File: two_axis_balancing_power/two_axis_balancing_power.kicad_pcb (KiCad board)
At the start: 4 copper layers, 50 x 42.9 mm, 26 parts, among them J1 Conn_01x02, J2 Conn_02x05, J3 Conn_01x02, Q1 AO3401A, U1 RPL-1.0-R, U2 LM393, U3 TB6612FNG

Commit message: Almost finished pcb
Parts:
- added REF**: MountingHole_2.2mm_M2, MountingHole:MountingHole_2.2mm_M2, F.Cu at (174.2, 87.2)
- added REF**: MountingHole_2.2mm_M2, MountingHole:MountingHole_2.2mm_M2, F.Cu at (131.2, 87.2)
- added REF**: MountingHole_2.2mm_M2, MountingHole:MountingHole_2.2mm_M2, F.Cu at (174.2, 122.8)
- added REF**: MountingHole_2.2mm_M2, MountingHole:MountingHole_2.2mm_M2, F.Cu at (131.2, 122.8)
- moved J3 7.82 mm to (138.5, 93.7), turned to -90 degrees
- moved C6 3.54 mm to (152.4, 88.1), turned to -90 degrees
- moved C5 3.51 mm to (154.3, 88.0), turned to -90 degrees
- moved C2 2.63 mm to (151.3, 94.8)
- moved U3 2.63 mm to (146.7, 89.8)
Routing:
- net +5V: track 93.2 -> 87.6 mm
- net /MOTOR_N: track 7.73 -> 11.3 mm
- net /AIN2: track 34.3 -> 30.8 mm
- net /STBY: track 33.5 -> 31.2 mm
- net /PWMA: track 29.8 -> 27.8 mm
- net /MOTOR_P: track 9.99 -> 11.0 mm
- net /AIN1: track 27.8 -> 28.6 mm
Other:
- outline, holes or cut-outs redrawn

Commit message: Finished pcb
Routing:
- net GND: track 2.98 -> 120.5 mm, vias 2 -> 81

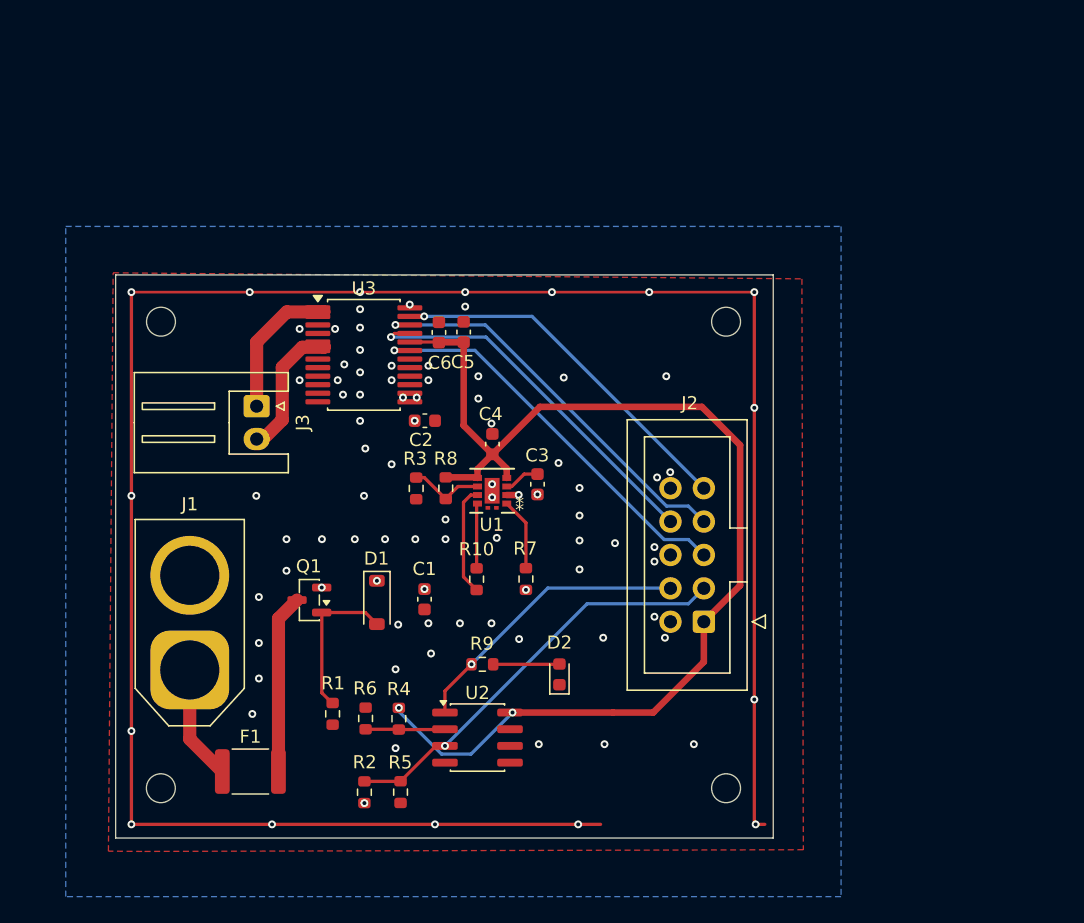
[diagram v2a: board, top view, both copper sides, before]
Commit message: Carrier schematic finished and power board polished
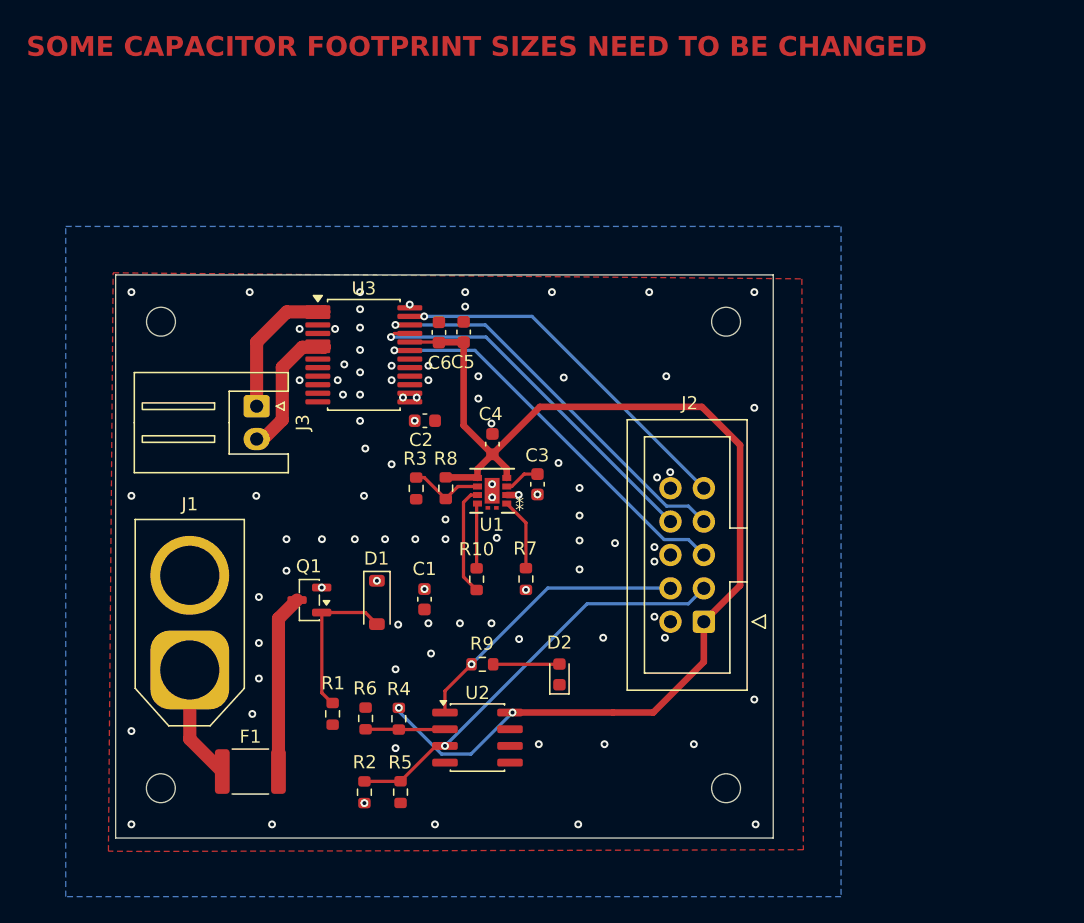
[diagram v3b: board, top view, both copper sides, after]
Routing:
- net GND: track 120.5 -> 3.22 mm
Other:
- board text added: "SOME CAPACITOR FOOTPRINT SIZES NEED TO BE CHANGED"

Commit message: Power actually finished; carrier pcb started
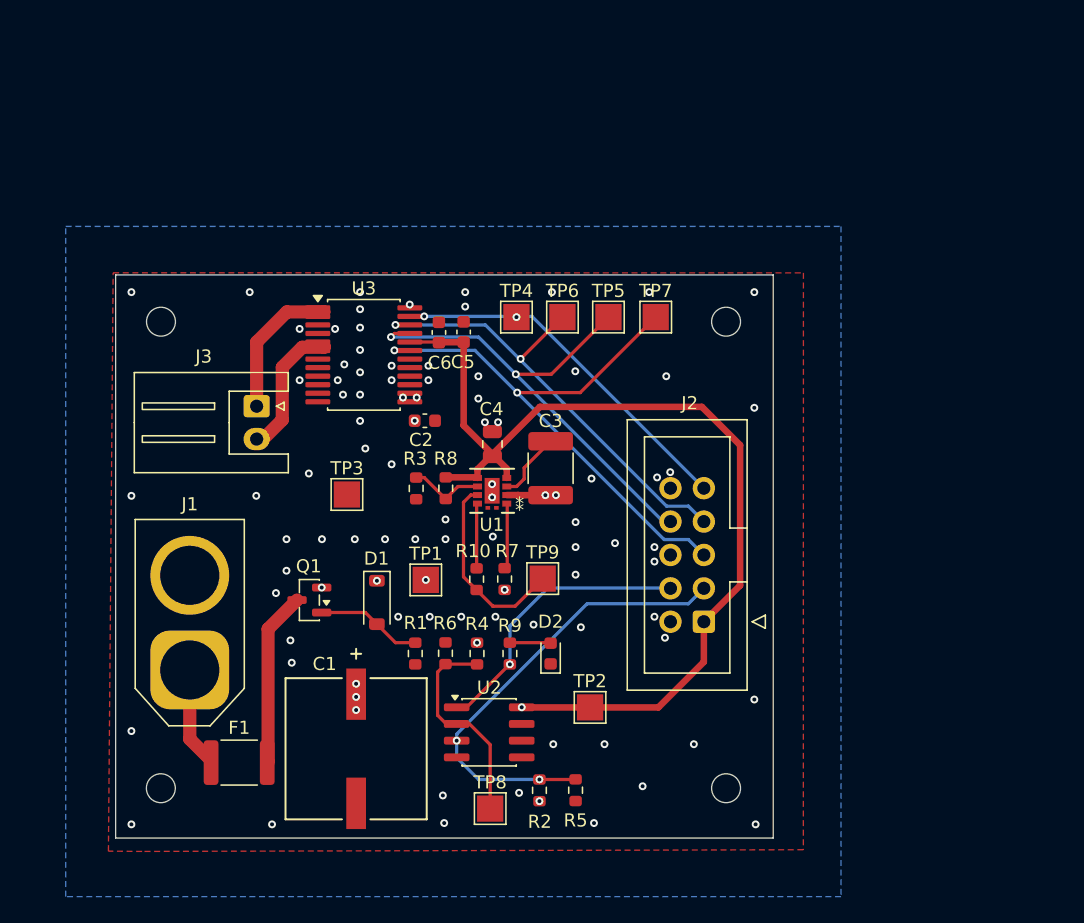
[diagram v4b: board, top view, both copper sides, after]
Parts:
- added TP1: TestPoint, TestPoint:TestPoint_Pad_2.0x2.0mm, F.Cu at (151.4, 106.9)
- added TP2: TestPoint, TestPoint:TestPoint_Pad_2.0x2.0mm, F.Cu at (163.9, 116.6)
- added TP3: TestPoint, TestPoint:TestPoint_Pad_2.0x2.0mm, F.Cu at (145.4, 100.4)
- added TP4: TestPoint, TestPoint:TestPoint_Pad_2.0x2.0mm, F.Cu at (158.3, 86.9)
- added TP5: TestPoint, TestPoint:TestPoint_Pad_2.0x2.0mm, F.Cu at (165.3, 86.9)
- added TP6: TestPoint, TestPoint:TestPoint_Pad_2.0x2.0mm, F.Cu at (161.8, 86.9)
- added TP7: TestPoint, TestPoint:TestPoint_Pad_2.0x2.0mm, F.Cu at (168.9, 86.9)
- added TP8: TestPoint, TestPoint:TestPoint_Pad_2.0x2.0mm, F.Cu at (156.3, 124.3)
- added TP9: TestPoint, TestPoint:TestPoint_Pad_2.0x2.0mm, F.Cu at (160.3, 106.8)
- C1: footprint Capacitor_SMD:C_0603_1608Metric -> 470uF SMD:PCAP_10x10-ELECT_NCA
- C3: footprint Capacitor_SMD:C_0603_1608Metric -> Capacitor_SMD:C_1812_4532Metric
- C4: footprint Capacitor_SMD:C_0603_1608Metric -> Capacitor_SMD:C_0805_2012Metric
- moved R2 13.3 mm to (160.1, 122.9)
- moved R5 13.3 mm to (162.8, 122.9)
- moved C1 12.5 mm to (146.1, 119.7)
- moved R6 7.85 mm to (152.9, 112.5)
- moved R1 7.79 mm to (150.6, 112.5)
- moved R4 7.75 mm to (155.3, 112.5)
- moved R9 2.25 mm to (157.8, 112.5), turned to -90 degrees
- moved D2 1.72 mm to (160.9, 112.5)
- moved R7 1.62 mm to (157.4, 106.8)
- moved C3 1.58 mm to (160.9, 98.4)
- moved F1 1.09 mm to (137.2, 120.8)
- moved U2 0.98 mm to (156.2, 118.5)
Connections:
- net Net-(U1-PG) renamed /Buck_PG
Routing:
- net VBAT: track 0.93 -> 19.0 mm, vias 11 -> 14
- net /STBY: track 31.2 -> 44.1 mm, vias 1 -> 2
- net /BAT_REF: track 6.03 -> 16.4 mm
- net /AIN1: track 28.6 -> 37.5 mm, vias 1 -> 2
- net /Buck_PG: track 8.38 -> 14.8 mm
- net +5V: track 87.6 -> 81.3 mm
- net /AIN2: track 30.8 -> 35.3 mm, vias 1 -> 2
- net Net-(D1-A): track 11.8 -> 8.08 mm
- net /BAT_LEV: track 31.9 -> 34.9 mm, vias 1 -> 2
- net GND: track 3.22 -> 5.75 mm, vias 81 -> 80
- net Net-(D2-A): track 5.05 -> 3.12 mm
- net Net-(J1-Pin_1): track 8.76 -> 7.72 mm
- net Net-(U1-CTRL): track 5.52 -> 5.01 mm
- net /PWMA: track 27.8 -> 27.9 mm, vias 1 -> 2
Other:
- board text removed: "SOME CAPACITOR FOOTPRINT SIZES NEED TO BE CHANGED"
